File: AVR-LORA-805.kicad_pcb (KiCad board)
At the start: 2 copper layers, 51.7 x 29.2 mm, 39 parts, among them J1 Batt, J2 Solar, J3 SMA, J4 CONN_01X14, J5 CONN_01X14, U1 MCP1700-3302E_SOT23, U2 RFM95HW, U3 AVR128DB28, Y1 24MHz, Y2 32768Hz

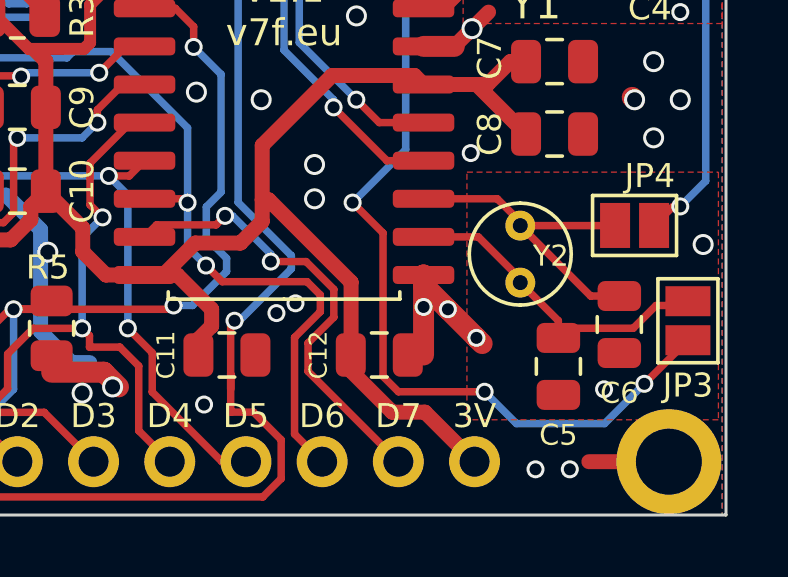
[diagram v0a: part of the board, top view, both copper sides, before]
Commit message: GND tracks
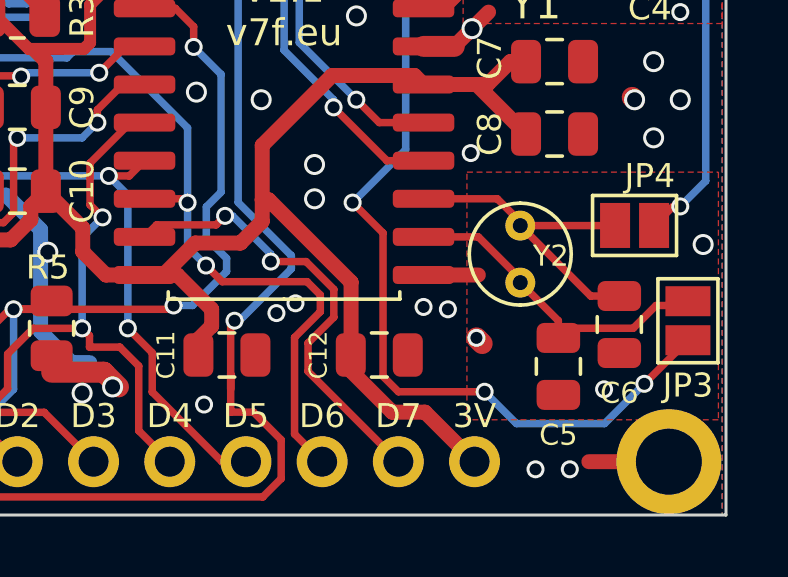
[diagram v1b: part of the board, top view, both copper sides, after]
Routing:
- net GND: track 71.2 -> 67.5 mm

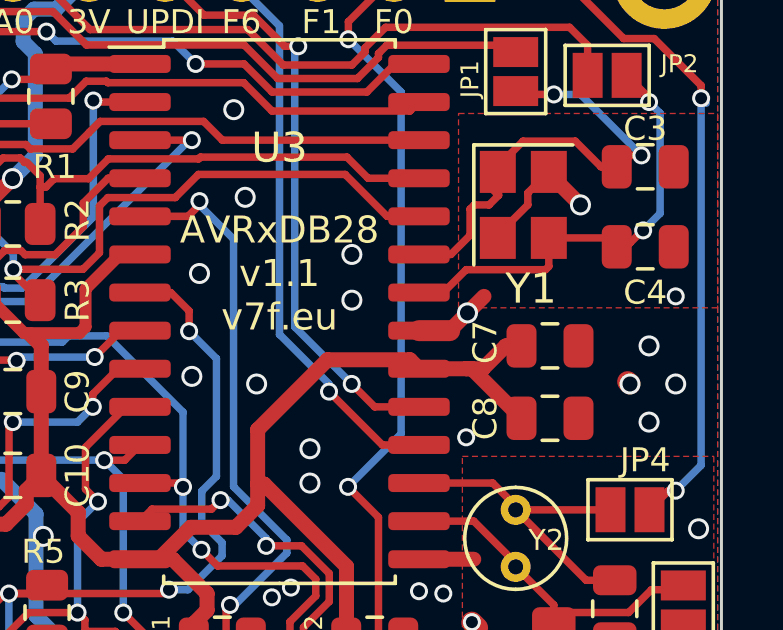
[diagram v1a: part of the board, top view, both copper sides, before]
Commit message: GND tracks
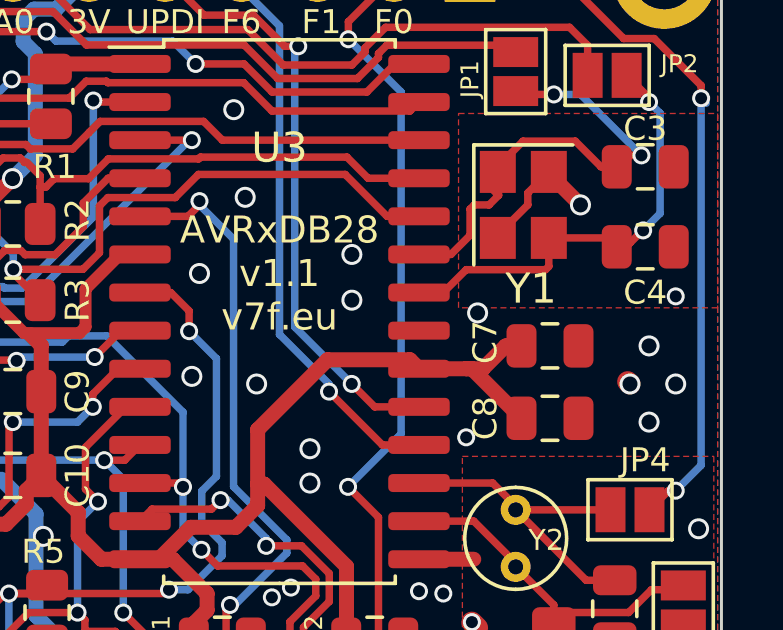
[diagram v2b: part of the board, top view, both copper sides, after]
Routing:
- net GND: track 67.5 -> 64.9 mm

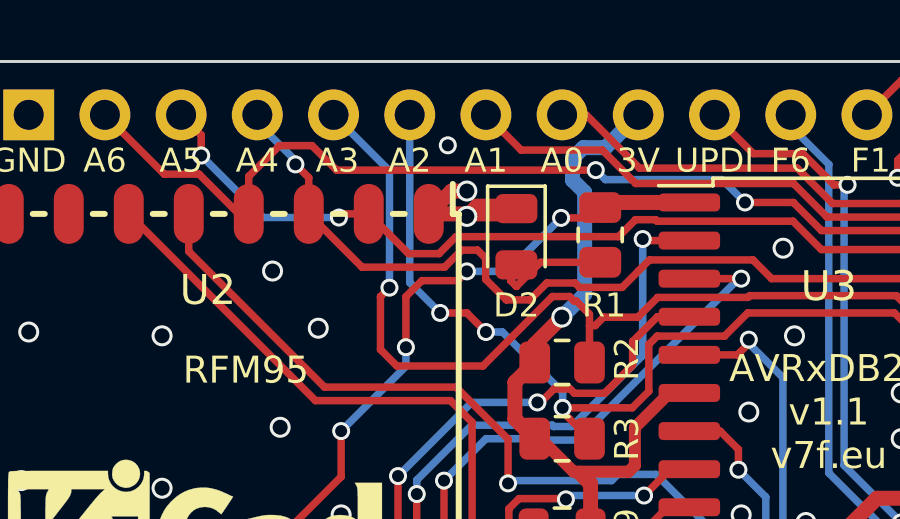
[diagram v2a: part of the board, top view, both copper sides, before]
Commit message: GND VIAs
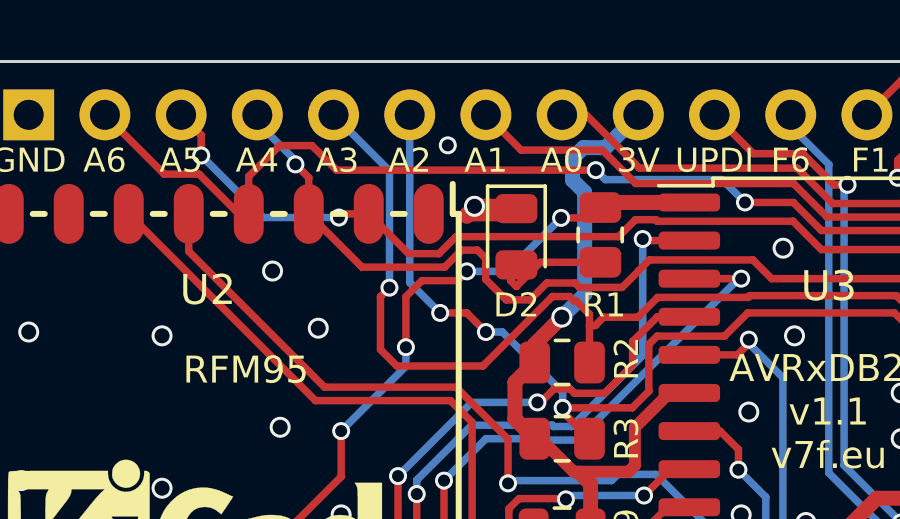
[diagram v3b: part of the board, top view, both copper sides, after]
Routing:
- net GND: track 64.9 -> 60.4 mm, vias 55 -> 54

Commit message: Kicad v9.0.0 version
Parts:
- D1: footprint Diode_SMD:D_SOT-23_ANK -> Package_TO_SOT_SMD:SOT-23
- moved D1 0.36 mm to (74.5, 84.2)
- moved REF** 0.11 mm to (69.5, 83.5)
- moved REF** 0.09 mm to (117.5, 109.0)
- moved REF** 0.09 mm to (69.6, 109.0)
- moved REF** 0.06 mm to (117.5, 83.5)
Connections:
- D1 pad 1: VCC -> Net-(D1-A)
- D1 pad 2: /Solar -> unconnected-(D1-K-Pad2)
- J2 pad 2: /Solar -> Net-(D1-A)
- U2 pad 11: Net-(U2-Pad11) -> unconnected-(U2-DIO3-Pad11)
- U2 pad 12: Net-(U2-Pad12) -> unconnected-(U2-DIO4-Pad12)
- U2 pad 7: Net-(U2-Pad7) -> unconnected-(U2-DIO5-Pad7)
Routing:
- net Net-(D1-A): track 0.00 -> 5.99 mm
- net /Solar: track 5.57 -> 0.00 mm
- net VCC: track 60.1 -> 58.7 mm
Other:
- net class Default removed
- net class Power removed
- board text added: "AVRxDB28 v1.2 v7f.eu"
- board text removed: "AVRxDB28 v1.1 v7f.eu"

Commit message: Minor cleanups AVR 805 version
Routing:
- net Net-(D2-A): track 4.00 -> 2.83 mm
- net GND: track 60.4 -> 59.7 mm
- net /A0: track 15.3 -> 14.7 mm
- net /C3: track 39.1 -> 38.6 mm
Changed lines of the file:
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@@
 			(net 37 "unconnected-(D1-K-Pad2)")
 			(pinfunction "K")
-			(pintype "passive")
+			(pintype "passive+no_connect")
 		)
 		(pad "3" smd roundrect
@@
 	)
 	(gr_text "UPDI"
-		(at 100.838 84.963 0)
+		(at 100.838 84.9 0)
 		(layer "F.SilkS")
 		(effects
 			(font
-				(size 0.8 0.8)
-				(thickness 0.15)
+				(size 0.6 0.6)
+				(thickness 0.1)
+				(bold yes)
 			)
 		)
@@
 	)
 	(gr_text "D4"
-		(at 100.838 107.188 180)
+		(at 100.838 107.1 180)
 		(layer "B.SilkS")
 		(effects
@@
 	)
 	(segment
-		(start 95.037 88.354)
-		(end 97.028 88.354)
-		(width 0.25)
-		(layer "F.Cu")
-		(net 1)
-	)
-	(segment
-		(start 94.234 89.157)
-		(end 94.237 89.157)
-		(width 0.25)
-		(layer "F.Cu")
-		(net 1)
-	)
-	(segment
-		(start 94.043032 88.631468)
+		(start 94.3205 88.354)
 		(end 94.234 88.4405)
 		(width 0.25)
@@
 	)
 	(segment
-		(start 94.234 89.157)
-		(end 94.043032 88.966032)
+		(start 97.028 88.354)
+		(end 94.3205 88.354)
 		(width 0.25)
 		(layer "F.Cu")
@@
 	)
 	(segment
-		(start 94.043032 88.966032)
-		(end 94.043032 88.631468)
-		(width 0.25)
-		(layer "F.Cu")
-		(net 1)
-	)
-	(segment
-		(start 94.234 89.157)
-		(end 95.037 88.354)
-		(width 0.25)
-		(layer "F.Cu")
-		(net 1)
-	)
-	(segment
-		(start 77.184 102.87)
-		(end 77.313 102.741)
-		(width 0.25)
-		(layer "F.Cu")
-		(net 2)
-	)
-	(segment
 		(start 75.678 100.711)
 		(end 72.009 100.711)
@@
 	)
 	(segment
-		(start 76.2 102.489)
-		(end 76.1365 102.4255)
-		(width 0.5)
-		(layer "F.Cu")
-		(net 4)
-	)
-	(segment
 		(start 94.234 86.484)
 		(end 92.922959 86.484)
@@
 	)
 	(segment
-		(start 75.692 101.981)
-		(end 76.1365 102.4255)
-		(width 0.5)
-		(layer "F.Cu")
-		(net 4)
-	)
-	(segment
 		(start 80.579 105.393)
 		(end 80.579 105.918)
@@
 	)
 	(segment
-		(start 76.1365 102.4255)
-		(end 75.946 102.235)
+		(start 75.692 101.981)
+		(end 76.2 102.489)
 		(width 0.5)
 		(layer "F.Cu")
@@
 	)
 	(segment
-		(start 111.926 91.759)
-		(end 111.926 92.159)
-		(width 0.25)
-		(layer "F.Cu")
-		(net 4)
-	)
-	(segment
 		(start 78.045393 104.453607)
 		(end 76.259607 104.453607)
@@
 	)
 	(segment
-		(start 78.154 105.918)
-		(end 78.0025 106.0695)
-		(width 0.5)
-		(layer "F.Cu")
-		(net 5)
-	)
-	(segment
 		(start 71.374 98.806)
 		(end 71.374 94.996)
@@
 	)
 	(segment
-		(start 69.849002 93.345)
-		(end 69.723 93.345)
-		(width 0.25)
-		(layer "F.Cu")
-		(net 5)
-	)
-	(segment
 		(start 70.898001 87.101999)
 		(end 72.987823 87.101999)
@@
 	)
 	(segment
-		(start 109.298 93.98)
-		(end 108.871232 93.98)
-		(width 0.25)
-		(layer "F.Cu")
-		(net 9)
-	)
-	(segment
-		(start 113.626 92.344002)
-		(end 113.626 92.159)
-		(width 0.25)
-		(layer "F.Cu")
-		(net 9)
-	)
-	(segment
 		(start 116.205 92.456)
 		(end 116.332 92.329)
@@
 	)
 	(segment
-		(start 112.537 87.376)
-		(end 112.522 87.391)
-		(width 0.25)
-		(layer "F.Cu")
-		(net 10)
-	)
-	(segment
 		(start 112.765999 88.933999)
 		(end 114.509999 88.933999)
@@
 	)
 	(segment
-		(start 101.727002 89.026998)
-		(end 101.727002 88.9)
-		(width 0.25)
-		(layer "B.Cu")
-		(net 16)
-	)
-	(segment
-		(start 85.598 109.093)
-		(end 85.679001 109.011999)
-		(width 0.25)
-		(layer "B.Cu")
-		(net 16)
-	)
-	(segment
 		(start 93.218 94.234)
 		(end 91.821 95.631)
@@
 	)
 	(segment
-		(start 102.86799 106.6794)
-		(end 102.86799 106.17401)
-		(width 0.25)
-		(layer "F.Cu")
-		(net 18)
-	)
-	(segment
 		(start 91.853001 110.268001)
 		(end 103.942001 110.268001)
@@
 	)
 	(segment
-		(start 103.378 109.093)
-		(end 103.03581 109.093)
-		(width 0.25)
-		(layer "F.Cu")
-		(net 23)
-	)
-	(segment
 		(start 100.253998 106.769996)
 		(end 100.253998 105.460998)
@@
 	)
 	(segment
-		(start 87.212996 86.741)
-		(end 87.313 86.741)
-		(width 0.25)
-		(layer "F.Cu")
-		(net 28)
-	)
-	(segment
 		(start 91.84113 88.516021)
 		(end 89.088021 88.516021)
@@
 	)
 	(segment
-		(start 96.6705 91.694)
-		(end 96.77441 91.694)
-		(width 0.25)
-		(layer "F.Cu")
-		(net 29)
-	)
-	(segment
 		(start 96.6705 90.464498)
 		(end 96.860502 90.464498)
@@
 	)
 	(segment
-		(start 116.0535 85.4465)
-		(end 116.121001 85.514001)
-		(width 0.25)
-		(layer "F.Cu")
-		(net 35)
-	)
-	(segment
 		(start 116.6465 85.4465)
 		(end 116.0535 85.4465)
@@
 		(net 35)
 	)
-	(segment
-		(start 118.703 87.503)
-		(end 118.872 87.672)
-		(width 0.25)
-		(layer "B.Cu")
-		(net 35)
-	)
